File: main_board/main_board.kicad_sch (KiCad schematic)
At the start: 32 parts, among them Q1 NMOS, U1 STM32G031G8Ux, U2 AMS1117-3.3

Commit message: feat(main_board/led): modify ohm for led
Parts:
- R1: value 100 -> 680
- R2, R4, R6: value 100 -> 0
- R3: value 100 -> 220
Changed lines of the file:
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@@
       (effects (font (size 1.27 1.27)))
     )
-    (property "Value" "100" (at 111.76 152.4 90)
+    (property "Value" "0" (at 111.76 152.4 90)
       (effects (font (size 1.27 1.27)))
     )
@@
       (effects (font (size 1.27 1.27)))
     )
-    (property "Value" "100" (at 111.76 143.51 90)
+    (property "Value" "220" (at 111.76 143.51 90)
       (effects (font (size 1.27 1.27)))
     )
@@
       (effects (font (size 1.27 1.27)))
     )
-    (property "Value" "100" (at 111.76 123.19 90)
+    (property "Value" "680" (at 111.76 123.19 90)
       (effects (font (size 1.27 1.27)))
     )
@@
       (effects (font (size 1.27 1.27)))
     )
-    (property "Value" "100" (at 111.76 132.08 90)
+    (property "Value" "0" (at 111.76 132.08 90)
       (effects (font (size 1.27 1.27)))
     )
@@
       (effects (font (size 1.27 1.27)))
     )
-    (property "Value" "100" (at 111.76 171.45 90)
-      (effects (font (size 1.27 1.27)))
-    )
+    (property "Value" "0" (at 111.76 171.45 90)
+      (effects (font (size 1.27 1.27)))
+    )

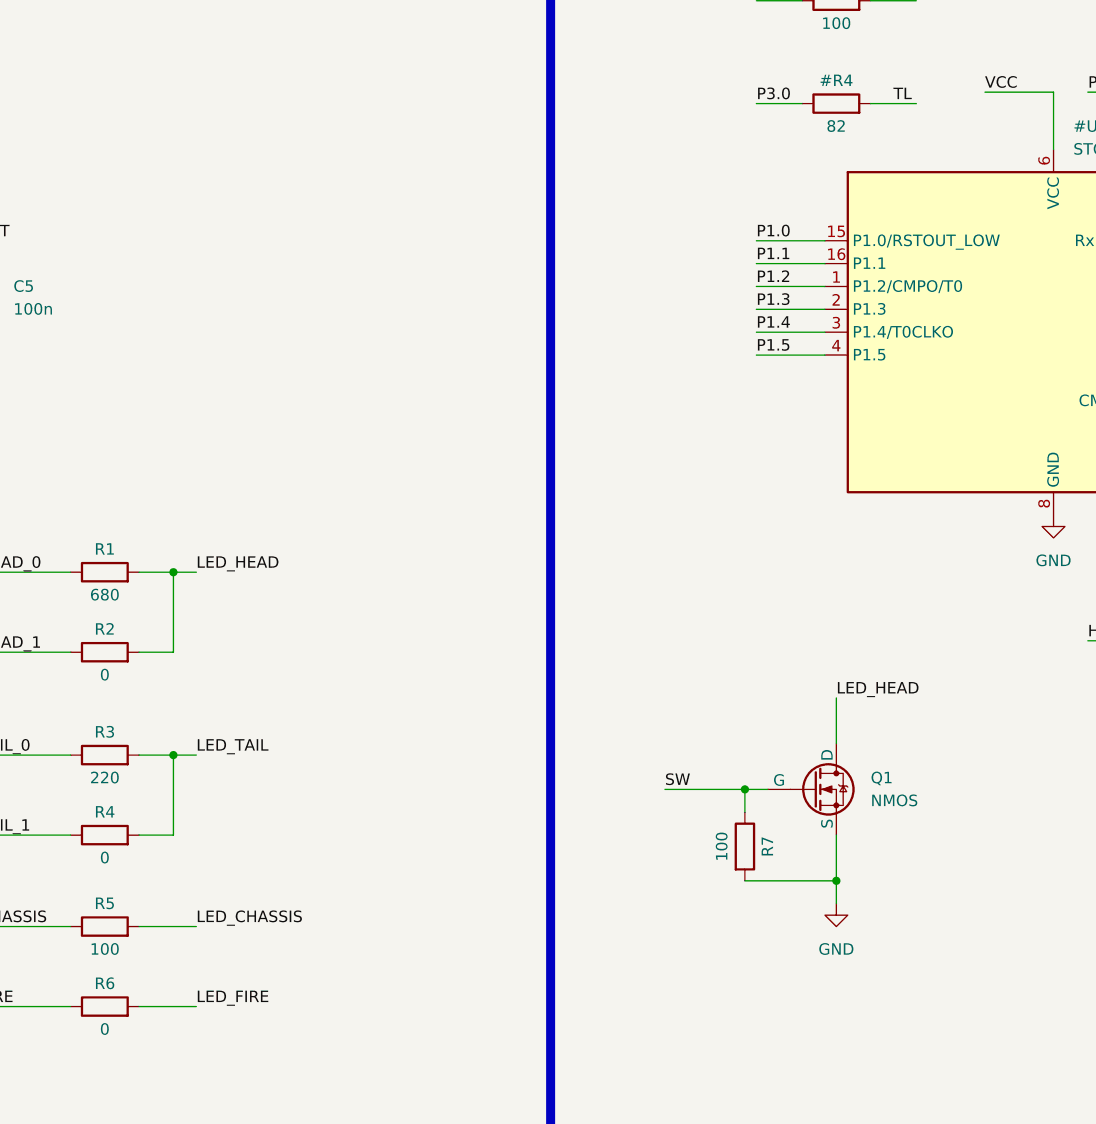
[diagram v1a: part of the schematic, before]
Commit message: feat(main_board/led): add MOSFET for led bar
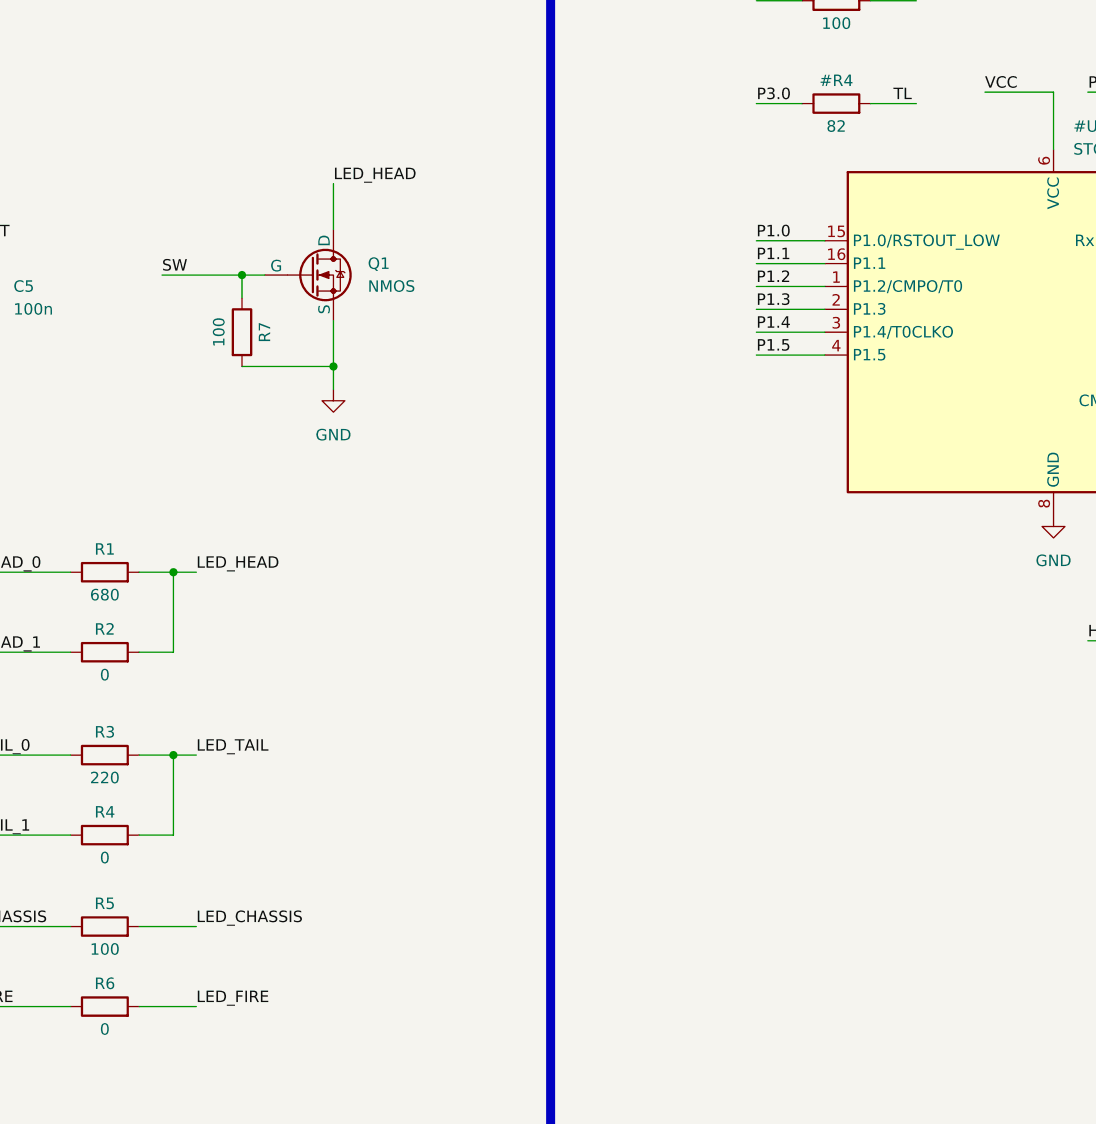
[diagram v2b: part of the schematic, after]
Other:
- moved on the sheet: Q1, R7
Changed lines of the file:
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@@
   (junction (at 119.38 140.97) (diameter 0) (color 0 0 0 0)
   )
-  (junction (at 193.04 154.94) (diameter 0) (color 0 0 0 0)
+  (junction (at 137.16 97.79) (diameter 0) (color 0 0 0 0)
   )
   (junction (at 50.8 58.42) (diameter 0) (color 0 0 0 0)
@@
   (junction (at 119.38 120.65) (diameter 0) (color 0 0 0 0)
   )
-  (junction (at 182.88 144.78) (diameter 0) (color 0 0 0 0)
+  (junction (at 127 87.63) (diameter 0) (color 0 0 0 0)
   )
   (no_connect (at 242.57 101.6))
@@
     (stroke (width 0) (type default))
   )
-  (wire (pts (xy 182.88 154.94) (xy 193.04 154.94))
+  (wire (pts (xy 127 97.79) (xy 137.16 97.79))
     (stroke (width 0) (type default))
   )
@@
     (stroke (width 0) (type default))
   )
-  (wire (pts (xy 193.04 154.94) (xy 193.04 157.48))
+  (wire (pts (xy 137.16 97.79) (xy 137.16 100.33))
     (stroke (width 0) (type default))
   )
@@
     (stroke (width 0) (type default))
   )
-  (wire (pts (xy 193.04 149.86) (xy 193.04 154.94))
+  (wire (pts (xy 137.16 92.71) (xy 137.16 97.79))
     (stroke (width 0) (type default))
   )
@@
     (stroke (width 0) (type default))
   )
-  (wire (pts (xy 182.88 147.32) (xy 182.88 144.78))
+  (wire (pts (xy 127 90.17) (xy 127 87.63))
     (stroke (width 0) (type default))
   )
@@
     (stroke (width 0) (type default))
   )
-  (wire (pts (xy 182.88 144.78) (xy 185.42 144.78))
+  (wire (pts (xy 127 87.63) (xy 129.54 87.63))
     (stroke (width 0) (type default))
   )
@@
     (stroke (width 0) (type default))
   )
-  (wire (pts (xy 182.88 144.78) (xy 173.99 144.78))
+  (wire (pts (xy 127 87.63) (xy 118.11 87.63))
     (stroke (width 0) (type default))
   )
@@
     (stroke (width 0) (type default))
   )
-  (wire (pts (xy 193.04 134.62) (xy 193.04 139.7))
+  (wire (pts (xy 137.16 77.47) (xy 137.16 82.55))
     (stroke (width 0) (type default))
   )
@@
     (effects (font (size 1.27 1.27)) (justify left bottom))
   )
-  (label "LED_HEAD" (at 193.04 134.62 0) (fields_autoplaced)
+  (label "LED_HEAD" (at 137.16 77.47 0) (fields_autoplaced)
     (effects (font (size 1.27 1.27)) (justify left bottom))
   )
@@
     (effects (font (size 1.27 1.27)) (justify left bottom))
   )
-  (label "SW" (at 173.99 144.78 0) (fields_autoplaced)
+  (label "SW" (at 118.11 87.63 0) (fields_autoplaced)
     (effects (font (size 1.27 1.27)) (justify left bottom))
   )
@@
     )
   )
-  (symbol (lib_id "Device:R") (at 182.88 151.13 0) (unit 1)
+  (symbol (lib_id "Device:R") (at 127 93.98 0) (unit 1)
     (in_bom yes) (on_board yes) (dnp no)
-    (property "Reference" "R7" (at 185.42 151.13 90)
-      (effects (font (size 1.27 1.27)))
-    )
-    (property "Value" "100" (at 180.34 151.13 90)
-      (effects (font (size 1.27 1.27)))
-    )
-    (property "Footprint" "Resistor_SMD:R_0402_1005Metric" (at 181.102 151.13 90)
-      (effects (font (size 1.27 1.27)) hide)
-    )
-    (property "Datasheet" "~" (at 182.88 151.13 0)
-      (effects (font (size 1.27 1.27)) hide)
-    )
-    (property "JLCPCB" "C25076" (at 182.88 151.13 0)
+    (property "Reference" "R7" (at 129.54 93.98 90)
+      (effects (font (size 1.27 1.27)))
+    )
+    (property "Value" "100" (at 124.46 93.98 90)
+      (effects (font (size 1.27 1.27)))
+    )
+    (property "Footprint" "Resistor_SMD:R_0402_1005Metric" (at 125.222 93.98 90)
+      (effects (font (size 1.27 1.27)) hide)
+    )
+    (property "Datasheet" "~" (at 127 93.98 0)
+      (effects (font (size 1.27 1.27)) hide)
+    )
+    (property "JLCPCB" "C25076" (at 127 93.98 0)
       (effects (font (size 1.27 1.27)) hide)
     )
@@
     )
   )
-  (symbol (lib_id "Simulation_SPICE:NMOS") (at 190.5 144.78 0) (unit 1)
-    (in_bom yes) (on_board yes) (dnp no) (fields_autoplaced)
-    (property "Reference" "Q1" (at 196.85 143.51 0)
-      (effects (font (size 1.27 1.27)) (justify left))
-    )
-    (property "Value" "NMOS" (at 196.85 146.05 0)
-      (effects (font (size 1.27 1.27)) (justify left))
-    )
-    (property "Footprint" "Package_TO_SOT_SMD:SOT-23" (at 195.58 142.24 0)
-      (effects (font (size 1.27 1.27)) hide)
-    )
-    (property "Datasheet" "https://ngspice.sourceforge.io/docs/ngspice-manual.pdf" (at 190.5 157.48 0)
-      (effects (font (size 1.27 1.27)) hide)
-    )
-    (property "Sim.Device" "NMOS" (at 190.5 161.925 0)
-      (effects (font (size 1.27 1.27)) hide)
-    )
-    (property "Sim.Type" "VDMOS" (at 190.5 163.83 0)
-      (effects (font (size 1.27 1.27)) hide)
-    )
-    (property "Sim.Pins" "1=D 2=G 3=S" (at 190.5 160.02 0)
-      (effects (font (size 1.27 1.27)) hide)
-    )
-    (property "JLCPCB" "C22463594" (at 190.5 144.78 0)
+  (symbol (lib_id "Simulation_SPICE:NMOS") (at 134.62 87.63 0) (unit 1)
+    (in_bom yes) (on_board yes) (dnp no) (fields_autoplaced)
+    (property "Reference" "Q1" (at 140.97 86.36 0)
+      (effects (font (size 1.27 1.27)) (justify left))
+    )
+    (property "Value" "NMOS" (at 140.97 88.9 0)
+      (effects (font (size 1.27 1.27)) (justify left))
+    )
+    (property "Footprint" "Package_TO_SOT_SMD:SOT-23" (at 139.7 85.09 0)
+      (effects (font (size 1.27 1.27)) hide)
+    )
+    (property "Datasheet" "https://ngspice.sourceforge.io/docs/ngspice-manual.pdf" (at 134.62 100.33 0)
+      (effects (font (size 1.27 1.27)) hide)
+    )
+    (property "Sim.Device" "NMOS" (at 134.62 104.775 0)
+      (effects (font (size 1.27 1.27)) hide)
+    )
+    (property "Sim.Type" "VDMOS" (at 134.62 106.68 0)
+      (effects (font (size 1.27 1.27)) hide)
+    )
+    (property "Sim.Pins" "1=D 2=G 3=S" (at 134.62 102.87 0)
+      (effects (font (size 1.27 1.27)) hide)
+    )
+    (property "JLCPCB" "C22463594" (at 134.62 87.63 0)
       (effects (font (size 1.27 1.27)) hide)
     )
@@
     )
   )
-  (symbol (lib_id "power:GND") (at 193.04 157.48 0) (unit 1)
-    (in_bom yes) (on_board yes) (dnp no) (fields_autoplaced)
-    (property "Reference" "#PWR016" (at 193.04 163.83 0)
-      (effects (font (size 1.27 1.27)) hide)
-    )
-    (property "Value" "GND" (at 193.04 162.56 0)
-      (effects (font (size 1.27 1.27)))
-    )
-    (property "Footprint" "" (at 193.04 157.48 0)
-      (effects (font (size 1.27 1.27)) hide)
-    )
-    (property "Datasheet" "" (at 193.04 157.48 0)
-      (effects (font (size 1.27 1.27)) hide)
-    )
+  (symbol (lib_id "power:GND") (at 137.16 100.33 0) (unit 1)
+    (in_bom yes) (on_board yes) (dnp no) (fields_autoplaced)
+    (property "Reference" "#PWR016" (at 137.16 106.68 0)
+      (effects (font (size 1.27 1.27)) hide)
+    )
+    (property "Value" "GND" (at 137.16 105.41 0)
+      (effects (font (size 1.27 1.27)))
+    )
+    (property "Footprint" "" (at 137.16 100.33 0)
+      (effects (font (size 1.27 1.27)) hide)
+    )
+    (property "Datasheet" "" (at 137.16 100.33 0)
+      (effects (font (size 1.27 1.27)) hide)
+    )

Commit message: feat(main_board/led): 高release gerber
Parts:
- R1: JLCPCB C25076 -> C25130
- R2, R4, R6: JLCPCB C25076 -> C17168
- R3: JLCPCB C25076 -> C25091
- S2: JLCPCB (none) -> C722914
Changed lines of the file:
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@@
       (effects (font (size 1.27 1.27)) hide)
     )
-    (property "JLCPCB" "" (at 82.55 25.4 0)
+    (property "JLCPCB" "C722914" (at 82.55 25.4 0)
       (effects (font (size 1.27 1.27)) hide)
     )
@@
       (effects (font (size 1.27 1.27)) hide)
     )
-    (property "JLCPCB" "C25076" (at 111.76 149.86 0)
+    (property "JLCPCB" "C17168" (at 111.76 149.86 0)
       (effects (font (size 1.27 1.27)) hide)
     )
@@
       (effects (font (size 1.27 1.27)) hide)
     )
-    (property "JLCPCB" "C25076" (at 111.76 140.97 0)
+    (property "JLCPCB" "C25091" (at 111.76 140.97 0)
       (effects (font (size 1.27 1.27)) hide)
     )
@@
       (effects (font (size 1.27 1.27)) hide)
     )
-    (property "JLCPCB" "C25076" (at 111.76 120.65 0)
+    (property "JLCPCB" "C25130" (at 111.76 120.65 0)
       (effects (font (size 1.27 1.27)) hide)
     )
@@
       (effects (font (size 1.27 1.27)) hide)
     )
-    (property "JLCPCB" "C25076" (at 111.76 129.54 0)
+    (property "JLCPCB" "C17168" (at 111.76 129.54 0)
       (effects (font (size 1.27 1.27)) hide)
     )
@@
       (effects (font (size 1.27 1.27)) hide)
     )
-    (property "JLCPCB" "C25076" (at 111.76 168.91 0)
-      (effects (font (size 1.27 1.27)) hide)
-    )
+    (property "JLCPCB" "C17168" (at 111.76 168.91 0)
+      (effects (font (size 1.27 1.27)) hide)
+    )
